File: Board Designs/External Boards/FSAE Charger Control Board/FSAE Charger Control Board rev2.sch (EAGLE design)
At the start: 38 parts, among them X1 CONNECTOR-4, X2 CONNECTOR-12

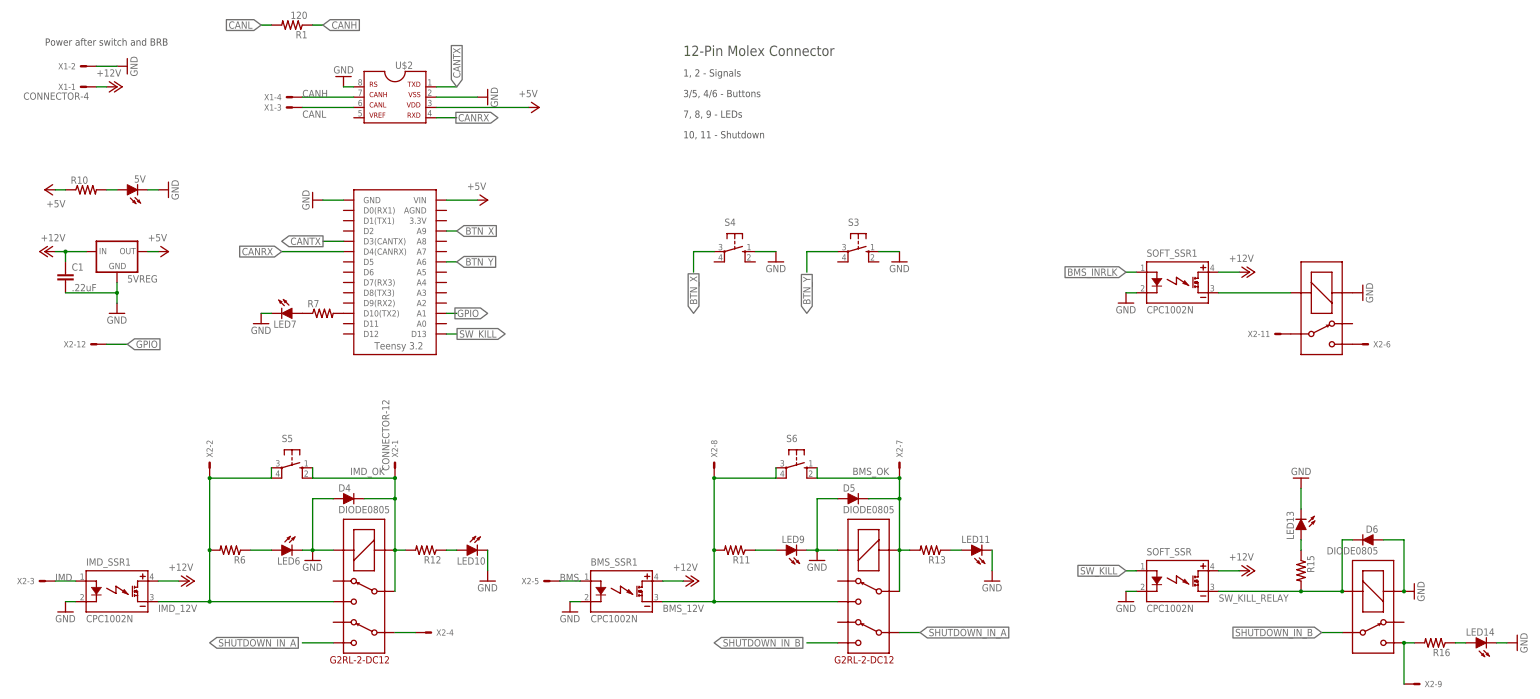
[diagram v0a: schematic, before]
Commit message: Added resistors to SSRs
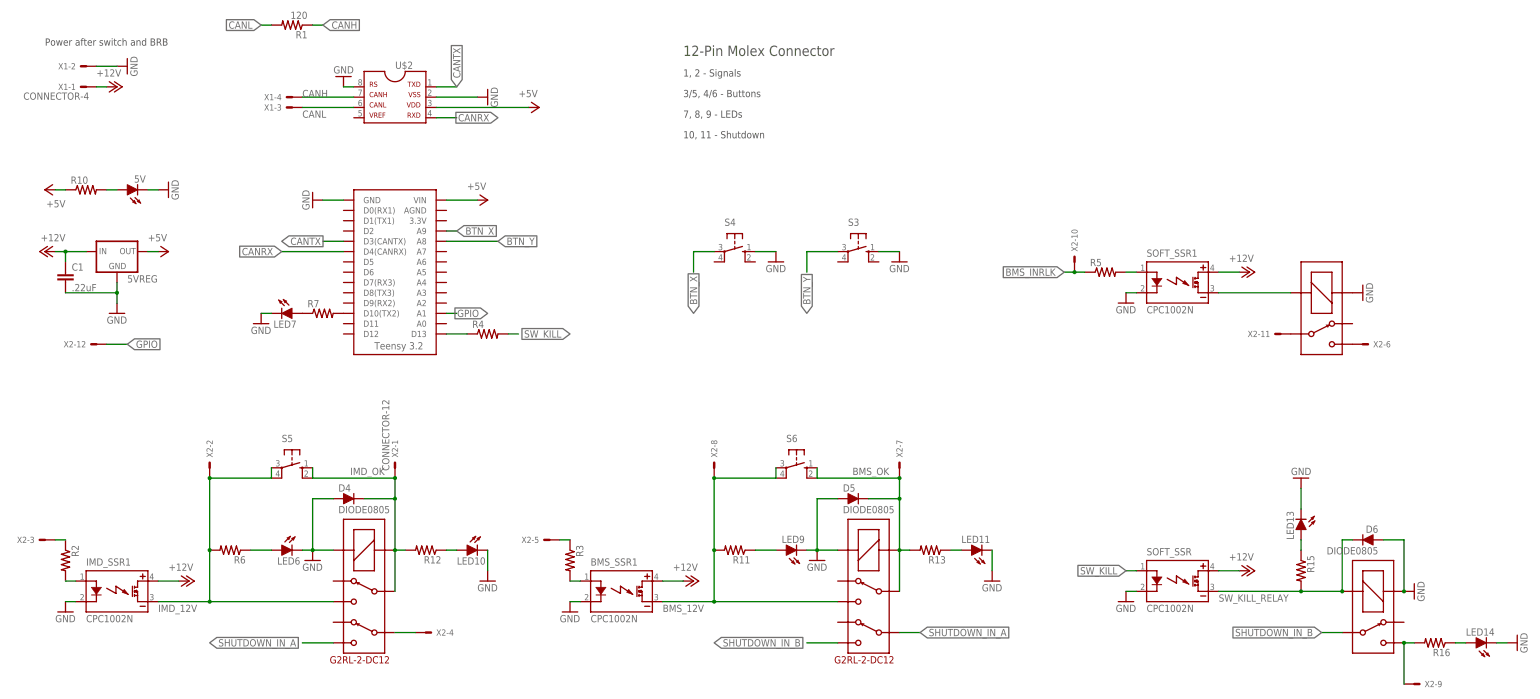
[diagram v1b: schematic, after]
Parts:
- added R2, R3, R4, R5: (no value), HyTechDevices:RESISTOR0805-RES
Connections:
- removed net BMS: BMS_SSR1.CONTROL+, X2-5.S
- removed net IMD: IMD_SSR1.CONTROL+, X2-3.S
- new net N$11: BMS_SSR1.CONTROL+, R3.2
- new net N$15: R2.1, X2-3.S
- new net N$16: R3.1, X2-5.S
- new net N$17: R5.2, SOFT_SSR1.CONTROL+
- new net N$18: R4.1, U$1.D13
- new net N$4: IMD_SSR1.CONTROL+, R2.2
- net BMS_INRLK: now also R5.1, X2-10.S; no longer SOFT_SSR1.CONTROL+
- net BTN_Y: now also U$1.A8; no longer U$1.A6
- net SW_KILL: now also R4.2; no longer U$1.D13
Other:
- moved on the sheet: X2-3, X2-5
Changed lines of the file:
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@@
 <part name="U$3" library="HyTechDevices" deviceset="G5LE" device=""/>
 <part name="GND8" library="supply1" deviceset="GND" device=""/>
+<part name="R2" library="HyTechDevices" deviceset="RESISTOR" device="0805-RES"/>
+<part name="R3" library="HyTechDevices" deviceset="RESISTOR" device="0805-RES"/>
+<part name="R5" library="HyTechDevices" deviceset="RESISTOR" device="0805-RES"/>
+<part name="R4" library="HyTechDevices" deviceset="RESISTOR" device="0805-RES"/>
 </parts>
 <sheets>
@@
 <instance part="GND8" gate="1" x="261.62" y="121.92" rot="R90"/>
 <instance part="X2" gate="-12" x="-50.8" y="109.22" rot="R180"/>
-<instance part="X2" gate="-5" x="60.96" y="50.8" rot="R180"/>
-<instance part="X2" gate="-3" x="-63.5" y="50.8" rot="R180"/>
+<instance part="X2" gate="-5" x="60.96" y="60.96" rot="R180"/>
+<instance part="X2" gate="-3" x="-63.5" y="60.96" rot="R180"/>
 <instance part="X2" gate="-1" x="22.86" y="78.74" rot="R90"/>
 <instance part="X2" gate="-7" x="147.32" y="78.74" rot="R90"/>
@@
 <instance part="X2" gate="-11" x="241.3" y="111.76" rot="R180"/>
 <instance part="X2" gate="-6" x="261.62" y="109.22"/>
+<instance part="R2" gate="G$1" x="-58.42" y="55.88" rot="R270"/>
+<instance part="R3" gate="G$1" x="66.04" y="55.88" rot="R270"/>
+<instance part="R5" gate="G$1" x="198.12" y="127"/>
+<instance part="X2" gate="-10" x="190.5" y="129.54" rot="R90"/>
+<instance part="R4" gate="G$1" x="45.72" y="111.76"/>
 </instances>
 <busses>
@@
 </segment>
 <segment>
-<label x="38.1" y="129.54" size="1.778" layer="95" xref="yes"/>
-<pinref part="U$1" gate="G$1" pin="A6"/>
-<wire x1="38.1" y1="129.54" x2="35.56" y2="129.54" width="0.1524" layer="91"/>
-</segment>
-</net>
-<net name="IMD" class="0">
-<segment>
-<pinref part="IMD_SSR1" gate="G$1" pin="CONTROL+"/>
-<wire x1="-60.96" y1="50.8" x2="-55.88" y2="50.8" width="0.1524" layer="91"/>
-<label x="-60.96" y="50.8" size="1.778" layer="95"/>
-<pinref part="X2" gate="-3" pin="S"/>
+<label x="48.26" y="134.62" size="1.778" layer="95" xref="yes"/>
+<wire x1="48.26" y1="134.62" x2="35.56" y2="134.62" width="0.1524" layer="91"/>
+<pinref part="U$1" gate="G$1" pin="A8"/>
 </segment>
 </net>
@@
 <wire x1="-7.62" y1="187.96" x2="-10.16" y2="187.96" width="0.1524" layer="91"/>
 <label x="-10.16" y="187.96" size="1.778" layer="95" rot="R180" xref="yes"/>
-</segment>
-</net>
-<net name="BMS" class="0">
-<segment>
-<pinref part="BMS_SSR1" gate="G$1" pin="CONTROL+"/>
-<wire x1="63.5" y1="50.8" x2="68.58" y2="50.8" width="0.1524" layer="91"/>
-<label x="63.5" y="50.8" size="1.778" layer="95"/>
-<pinref part="X2" gate="-5" pin="S"/>
 </segment>
 </net>
@@
 <net name="SW_KILL" class="0">
 <segment>
-<label x="50.038" y="111.76" size="1.778" layer="95" rot="R180" xref="yes"/>
-<pinref part="U$1" gate="G$1" pin="D13"/>
-<wire x1="38.1" y1="111.76" x2="35.56" y2="111.76" width="0.1524" layer="91"/>
-</segment>
-<segment>
 <pinref part="SOFT_SSR" gate="G$1" pin="CONTROL+"/>
 <wire x1="205.74" y1="53.34" x2="203.2" y2="53.34" width="0.1524" layer="91"/>
 <label x="203.2" y="53.34" size="1.778" layer="95" rot="R180" xref="yes"/>
+</segment>
+<segment>
+<pinref part="R4" gate="G$1" pin="2"/>
+<wire x1="50.8" y1="111.76" x2="53.34" y2="111.76" width="0.1524" layer="91"/>
+<label x="66.04" y="111.76" size="1.778" layer="95" rot="R180" xref="yes"/>
 </segment>
 </net>
@@
 </segment>
 </net>
-<net name="BMS_INRLK" class="0">
-<segment>
-<pinref part="SOFT_SSR1" gate="G$1" pin="CONTROL+"/>
-<wire x1="205.74" y1="127" x2="203.2" y2="127" width="0.1524" layer="91"/>
-<label x="203.2" y="127" size="1.778" layer="95" rot="R180" xref="yes"/>
-</segment>
-</net>
 <net name="N$1" class="0">
 <segment>
@@
 </segment>
 </net>
+<net name="N$4" class="0">
+<segment>
+<pinref part="IMD_SSR1" gate="G$1" pin="CONTROL+"/>
+<pinref part="R2" gate="G$1" pin="2"/>
+<wire x1="-58.42" y1="50.8" x2="-55.88" y2="50.8" width="0.1524" layer="91"/>
+</segment>
+</net>
+<net name="N$11" class="0">
+<segment>
+<pinref part="BMS_SSR1" gate="G$1" pin="CONTROL+"/>
+<pinref part="R3" gate="G$1" pin="2"/>
+<wire x1="66.04" y1="50.8" x2="68.58" y2="50.8" width="0.1524" layer="91"/>
+</segment>
+</net>
+<net name="N$15" class="0">
+<segment>
+<pinref part="R2" gate="G$1" pin="1"/>
+<pinref part="X2" gate="-3" pin="S"/>
+<wire x1="-60.96" y1="60.96" x2="-58.42" y2="60.96" width="0.1524" layer="91"/>
+</segment>
+</net>
+<net name="N$16" class="0">
+<segment>
+<pinref part="R3" gate="G$1" pin="1"/>
+<pinref part="X2" gate="-5" pin="S"/>
+<wire x1="63.5" y1="60.96" x2="66.04" y2="60.96" width="0.1524" layer="91"/>
+</segment>
+</net>
+<net name="N$17" class="0">
+<segment>
+<pinref part="SOFT_SSR1" gate="G$1" pin="CONTROL+"/>
+<pinref part="R5" gate="G$1" pin="2"/>
+<wire x1="203.2" y1="127" x2="205.74" y2="127" width="0.1524" layer="91"/>
+</segment>
+</net>
+<net name="BMS_INRLK" class="0">
+<segment>
+<pinref part="R5" gate="G$1" pin="1"/>
+<wire x1="193.04" y1="127" x2="190.5" y2="127" width="0.1524" layer="91"/>
+<label x="187.96" y="127" size="1.778" layer="95" rot="R180" xref="yes"/>
+<pinref part="X2" gate="-10" pin="S"/>
+<wire x1="190.5" y1="127" x2="187.96" y2="127" width="0.1524" layer="91"/>
+<junction x="190.5" y="127"/>
+</segment>
+</net>
+<net name="N$18" class="0">
+<segment>
+<pinref part="U$1" gate="G$1" pin="D13"/>
+<wire x1="35.56" y1="111.76" x2="40.64" y2="111.76" width="0.1524" layer="91"/>
+<pinref part="R4" gate="G$1" pin="1"/>
+</segment>
+</net>
